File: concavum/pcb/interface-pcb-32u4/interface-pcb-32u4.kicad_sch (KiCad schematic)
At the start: 22 parts, among them J1 USB_C_Port, J2 Audio_Jack, J3 ISP_pads, J4 FPC_connector, U1 ATmega32U4-A, U2 MCP23017_SO, Y1 Crystal_16MHz

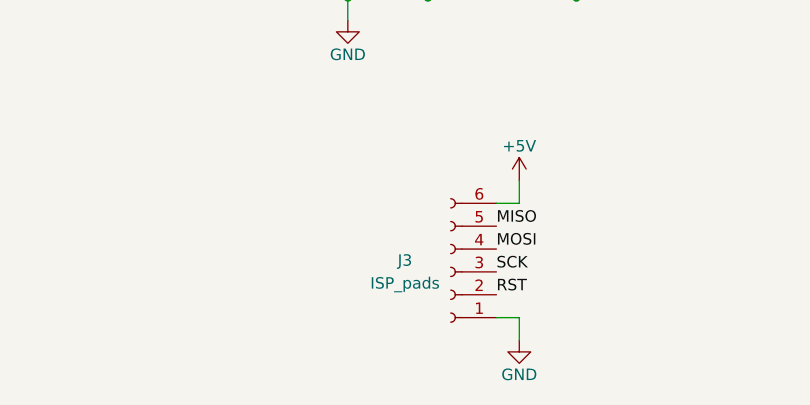
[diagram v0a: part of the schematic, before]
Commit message: Rename footprints to match KiCad naming scheme
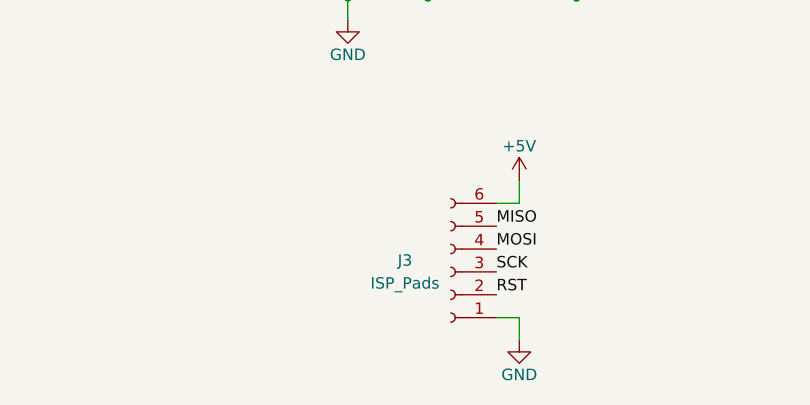
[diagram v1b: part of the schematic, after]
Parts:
- J2: footprint Custom:Audio-Jack-Dual-Side -> Custom:Audio_Jack_Dual_Side
- J3: value ISP_pads -> ISP_Pads; footprint Custom:ISP-Pads -> Custom:ISP_Pads
- J4: footprint Custom:FPC-Connector -> Custom:FPC_Connector
- U1: footprint Custom:TQFP-44-Rounded-Pads -> Custom:TQFP_44_Rounded_Pads
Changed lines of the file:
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@@
       (effects (font (size 1.27 1.27)) (justify left))
     )
-    (property "Footprint" "Custom:FPC-Connector" (id 2) (at 238.76 124.46 0)
+    (property "Footprint" "Custom:FPC_Connector" (id 2) (at 238.76 124.46 0)
       (effects (font (size 1.27 1.27)) hide)
     )
@@
       (effects (font (size 1.27 1.27)) (justify left))
     )
-    (property "Footprint" "Custom:TQFP-44-Rounded-Pads" (id 2) (at 151.13 82.55 0)
+    (property "Footprint" "Custom:TQFP_44_Rounded_Pads" (id 2) (at 151.13 82.55 0)
       (effects (font (size 1.27 1.27) italic) hide)
     )
@@
     (property "Reference" "J2" (id 0) (at 64.135 99.06 0))
     (property "Value" "Audio_Jack" (id 1) (at 64.135 101.6 0))
-    (property "Footprint" "Custom:Audio-Jack-Dual-Side" (id 2) (at 66.04 107.95 0)
+    (property "Footprint" "Custom:Audio_Jack_Dual_Side" (id 2) (at 66.04 107.95 0)
       (effects (font (size 1.27 1.27)) hide)
     )
@@
     (in_bom yes) (on_board yes)
     (property "Reference" "J3" (id 0) (at 129.54 160.02 0))
-    (property "Value" "ISP_pads" (id 1) (at 129.54 162.56 0))
-    (property "Footprint" "Custom:ISP-Pads" (id 2) (at 134.62 161.29 0)
+    (property "Value" "ISP_Pads" (id 1) (at 129.54 162.56 0))
+    (property "Footprint" "Custom:ISP_Pads" (id 2) (at 134.62 161.29 0)
       (effects (font (size 1.27 1.27)) hide)
     )
@@
     )
     (path "/6a3147f7-4763-47a0-97d1-d1711a55bb9d"
-      (reference "J2") (unit 1) (value "Audio_Jack") (footprint "Custom:Audio-Jack-Dual-Side")
+      (reference "J2") (unit 1) (value "Audio_Jack") (footprint "Custom:Audio_Jack_Dual_Side")
     )
     (path "/b2676d98-45fd-4fbc-be14-66c9e122701b"
-      (reference "J3") (unit 1) (value "ISP_pads") (footprint "Custom:ISP-Pads")
+      (reference "J3") (unit 1) (value "ISP_Pads") (footprint "Custom:ISP_Pads")
     )
     (path "/44d37f7c-27b7-4246-9e5b-dfcd81b85bf8"
-      (reference "J4") (unit 1) (value "FPC_connector") (footprint "Custom:FPC-Connector")
+      (reference "J4") (unit 1) (value "FPC_connector") (footprint "Custom:FPC_Connector")
     )
     (path "/13621f30-38eb-438c-99e2-f2bda3f08c97"
@@
     )
     (path "/4e171e27-0952-4a5f-bd26-afc8662a6d9a"
-      (reference "U1") (unit 1) (value "ATmega32U4-A") (footprint "Custom:TQFP-44-Rounded-Pads")
+      (reference "U1") (unit 1) (value "ATmega32U4-A") (footprint "Custom:TQFP_44_Rounded_Pads")
     )
     (path "/48cffc50-fb06-4eb1-9b93-78f85a43b110"

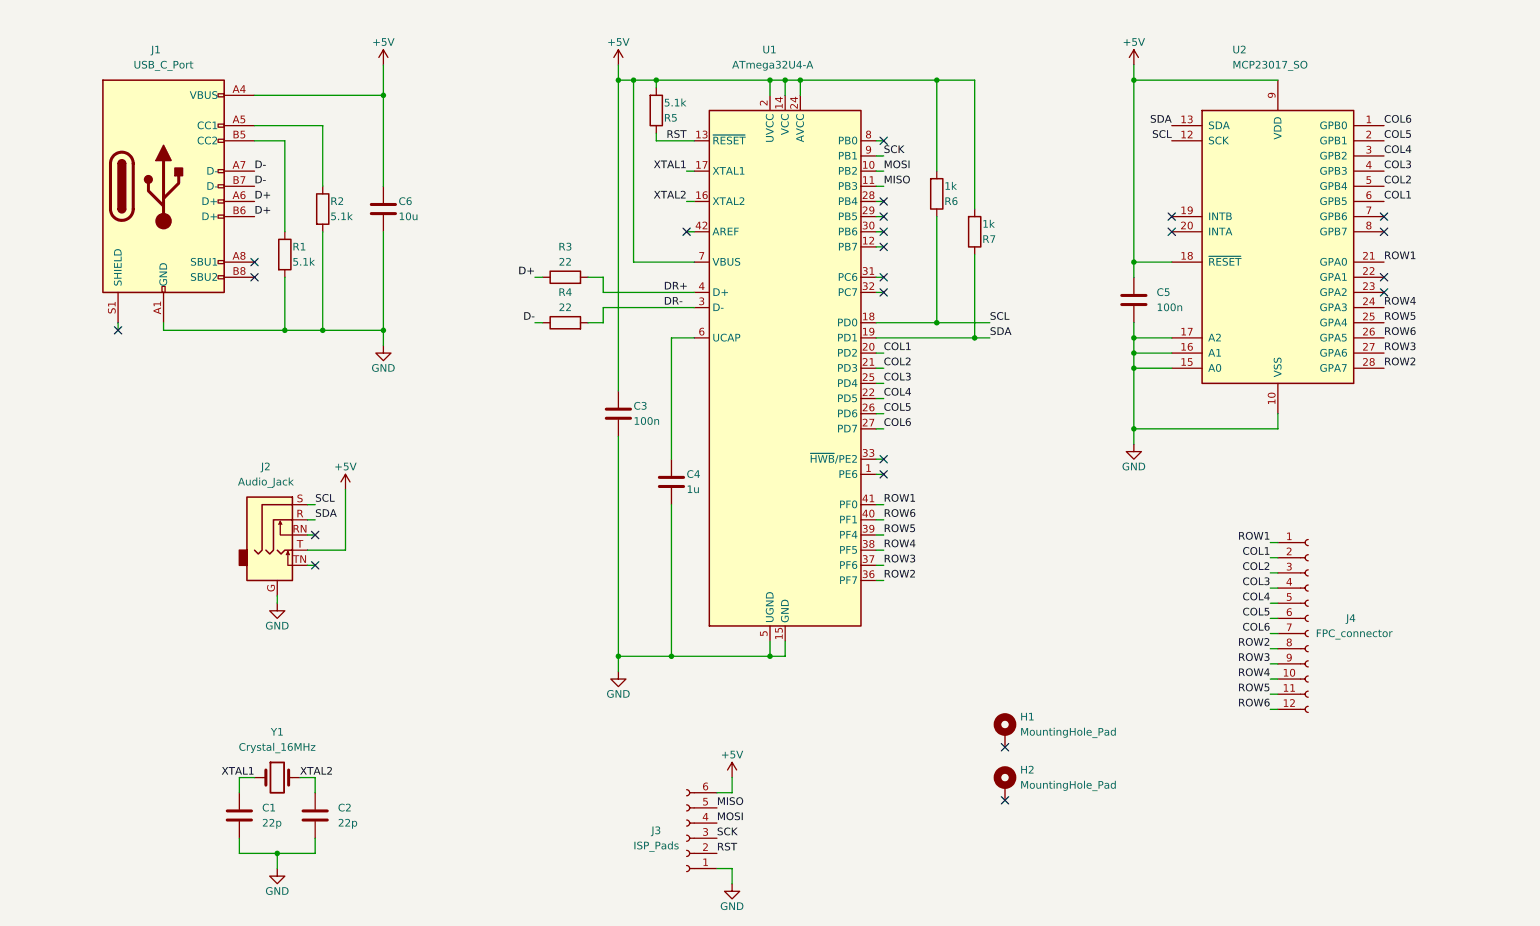
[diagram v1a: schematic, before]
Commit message: Add labels to show the half elements correspond to
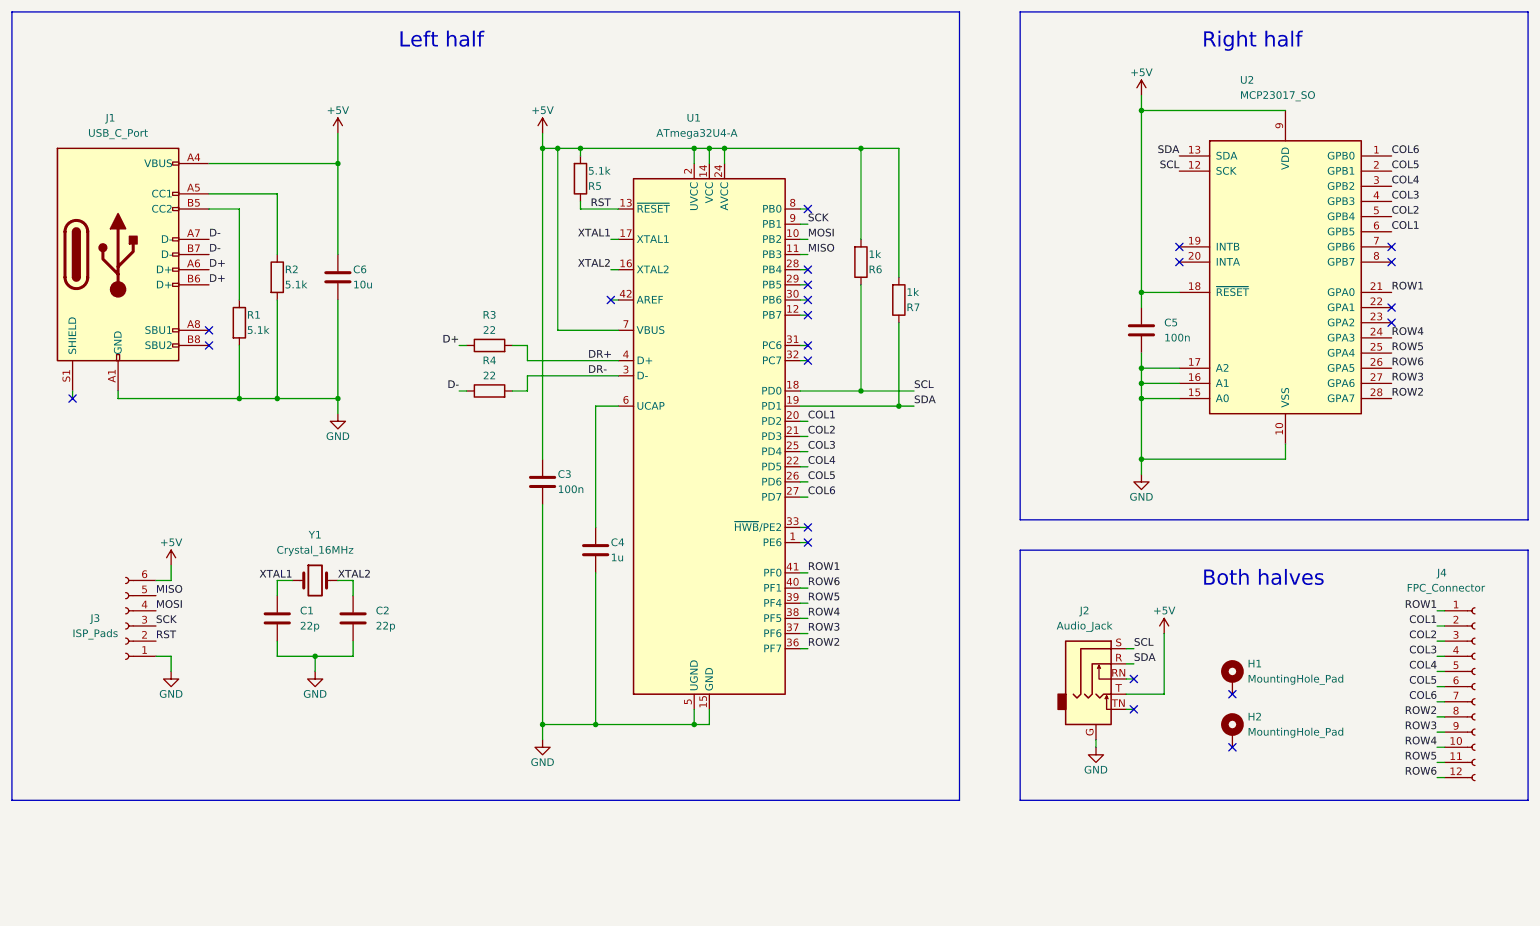
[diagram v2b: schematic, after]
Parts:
- J4: value FPC_connector -> FPC_Connector
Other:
- note added: "Both halves"
- note added: "Left half"
- note added: "Right half"
- moved on the sheet: C1, C2, C3, C4, C5, C6, H1, H2, J1, J2, J3, J4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

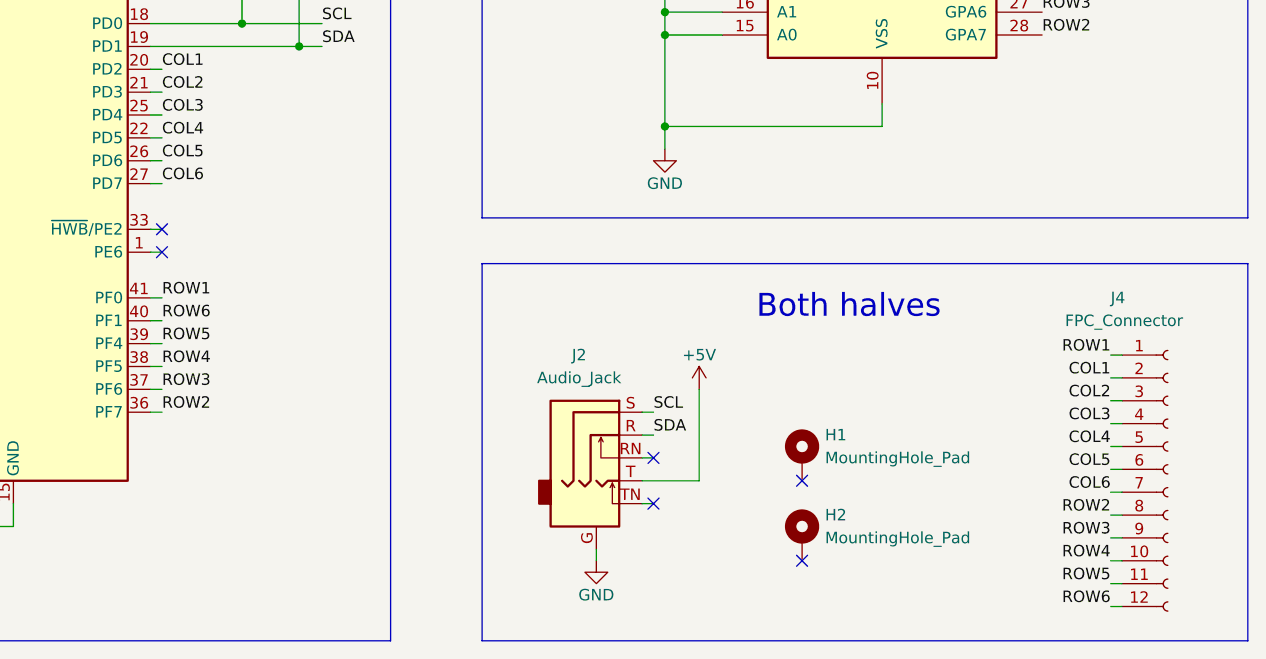
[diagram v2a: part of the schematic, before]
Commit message: Change FPC connector pinout to increase clearances
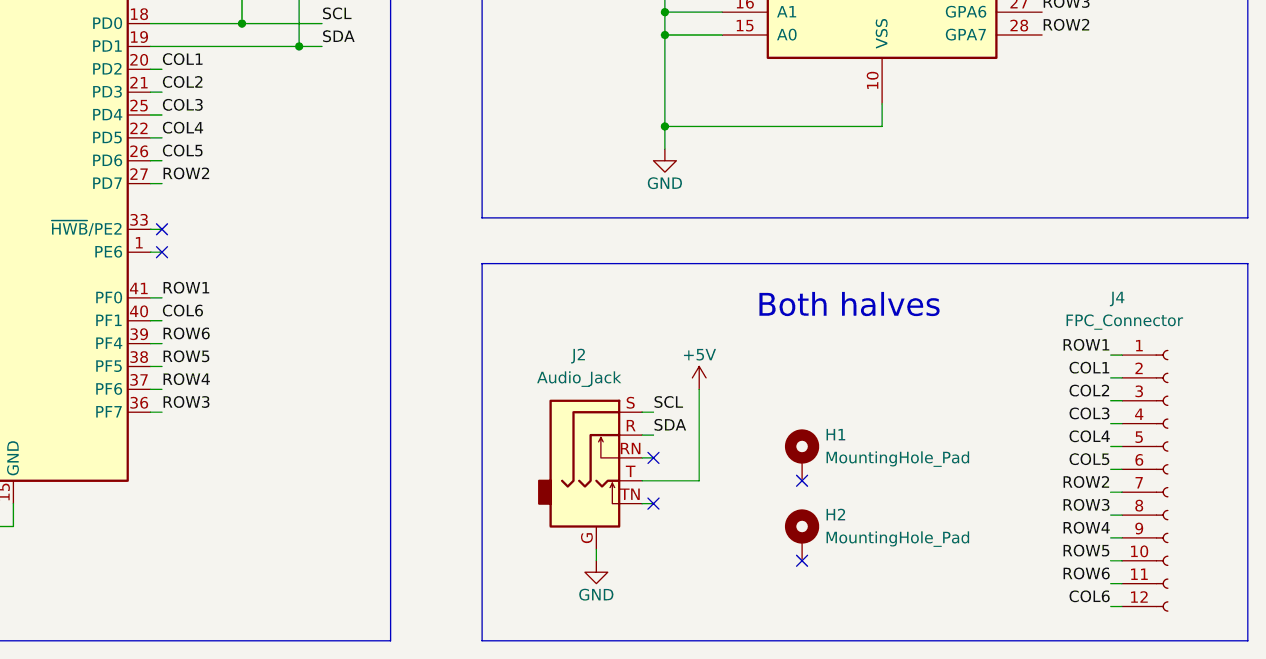
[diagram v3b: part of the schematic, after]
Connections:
- net COL6: now also J4.12 (Pin_12), U1.40 (PF1); no longer J4.7 (Pin_7), U1.27 (PD7)
- net ROW2: now also J4.7 (Pin_7), U1.27 (PD7); no longer J4.8 (Pin_8), U1.36 (PF7)
- net ROW3: now also J4.8 (Pin_8), U1.36 (PF7); no longer J4.9 (Pin_9), U1.37 (PF6)
- net ROW4: now also J4.9 (Pin_9), U1.37 (PF6); no longer J4.10 (Pin_10), U1.38 (PF5)
- net ROW5: now also J4.10 (Pin_10), U1.38 (PF5); no longer J4.11 (Pin_11), U1.39 (PF4)
- net ROW6: now also J4.11 (Pin_11), U1.39 (PF4); no longer J4.12 (Pin_12), U1.40 (PF1)
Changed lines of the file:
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@@
     (effects (font (size 1.27 1.27)) (justify left bottom))
   )
-  (label "ROW4" (at 154.94 124.46 0)
+  (label "ROW4" (at 154.94 127 0)
     (effects (font (size 1.27 1.27)) (justify left bottom))
   )
@@
     (effects (font (size 1.27 1.27)) (justify left bottom))
   )
-  (label "ROW3" (at 260.35 143.51 180)
+  (label "ROW3" (at 260.35 140.97 180)
     (effects (font (size 1.27 1.27)) (justify right bottom))
   )
@@
     (effects (font (size 1.27 1.27)) (justify left bottom))
   )
-  (label "COL6" (at 260.35 138.43 180)
+  (label "COL6" (at 260.35 151.13 180)
     (effects (font (size 1.27 1.27)) (justify right bottom))
   )
@@
     (effects (font (size 1.27 1.27)) (justify left bottom))
   )
-  (label "ROW6" (at 260.35 151.13 180)
+  (label "ROW6" (at 260.35 148.59 180)
     (effects (font (size 1.27 1.27)) (justify right bottom))
   )
@@
     (effects (font (size 1.27 1.27)) (justify right bottom))
   )
-  (label "ROW3" (at 154.94 127 0)
+  (label "ROW3" (at 154.94 129.54 0)
     (effects (font (size 1.27 1.27)) (justify left bottom))
   )
@@
     (effects (font (size 1.27 1.27)) (justify left bottom))
   )
-  (label "ROW2" (at 154.94 129.54 0)
+  (label "ROW2" (at 154.94 104.14 0)
     (effects (font (size 1.27 1.27)) (justify left bottom))
   )
@@
     (effects (font (size 1.27 1.27)) (justify right bottom))
   )
-  (label "ROW6" (at 154.94 119.38 0)
+  (label "ROW6" (at 154.94 121.92 0)
     (effects (font (size 1.27 1.27)) (justify left bottom))
   )
@@
     (effects (font (size 1.27 1.27)) (justify left bottom))
   )
-  (label "ROW2" (at 260.35 140.97 180)
+  (label "ROW2" (at 260.35 138.43 180)
     (effects (font (size 1.27 1.27)) (justify right bottom))
   )
@@
     (effects (font (size 1.27 1.27)) (justify left bottom))
   )
-  (label "ROW5" (at 260.35 148.59 180)
+  (label "ROW5" (at 260.35 146.05 180)
     (effects (font (size 1.27 1.27)) (justify right bottom))
   )
@@
     (effects (font (size 1.27 1.27)) (justify right bottom))
   )
-  (label "ROW4" (at 260.35 146.05 180)
+  (label "ROW4" (at 260.35 143.51 180)
     (effects (font (size 1.27 1.27)) (justify right bottom))
   )
@@
     (effects (font (size 1.27 1.27)) (justify right bottom))
   )
-  (label "ROW5" (at 154.94 121.92 0)
+  (label "ROW5" (at 154.94 124.46 0)
     (effects (font (size 1.27 1.27)) (justify left bottom))
   )
@@
     (effects (font (size 1.27 1.27)) (justify left bottom))
   )
-  (label "COL6" (at 154.94 104.14 0)
+  (label "COL6" (at 154.94 119.38 0)
     (effects (font (size 1.27 1.27)) (justify left bottom))
   )
